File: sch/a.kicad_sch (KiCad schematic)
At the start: 1 part

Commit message: Update
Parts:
- added L? (x2): L, symbol Device:L
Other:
- moved on the sheet: L?
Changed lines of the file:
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@@
 (kicad_sch (version 20211123) (generator eeschema)
   (paper "A4")
-  (symbol (lib_id "Device:L") (at 132.08 100.33 0) (unit 1)
+  (symbol (lib_id "Device:L") (at 153.67 110.49 0) (unit 1)
     (in_bom yes) (on_board yes) (fields_autoplaced)
-    (property "Reference" "L?" (id 0) (at 133.35 99.0599 0)
+    (property "Reference" "L?" (id 0) (at 154.94 109.2199 0)
       (effects (font (size 1.27 1.27)) (justify left))
     )
-    (property "Value" "L" (id 1) (at 133.35 101.5999 0)
+    (property "Value" "L" (id 1) (at 154.94 111.7599 0)
       (effects (font (size 1.27 1.27)) (justify left))
     )
-    (property "Footprint" "" (id 2) (at 132.08 100.33 0)
+    (property "Footprint" "" (id 2) (at 153.67 110.49 0)
       (effects (font (size 1.27 1.27)) hide)
     )
-    (property "Datasheet" "~" (id 3) (at 132.08 100.33 0)
+    (property "Datasheet" "~" (id 3) (at 153.67 110.49 0)
       (effects (font (size 1.27 1.27)) hide)
     )
@@
     (pin "2")
   )
-  (sheet (at 142.24 93.98) (size 40.64 21.59) (fields_autoplaced)
+  (symbol (lib_id "Device:L") (at 158.75 110.49 0) (unit 1)
+    (in_bom yes) (on_board yes) (fields_autoplaced)
+    (property "Reference" "L?" (id 0) (at 160.02 109.2199 0)
+      (effects (font (size 1.27 1.27)) (justify left))
+    )
+    (property "Value" "L" (id 1) (at 160.02 111.7599 0)
+      (effects (font (size 1.27 1.27)) (justify left))
+    )
+    (property "Footprint" "" (id 2) (at 158.75 110.49 0)
+      (effects (font (size 1.27 1.27)) hide)
+    )
+    (property "Datasheet" "~" (id 3) (at 158.75 110.49 0)
+      (effects (font (size 1.27 1.27)) hide)
+    )
+    (pin "1")
+    (pin "2")
+  )
+  (symbol (lib_id "Device:L") (at 147.32 110.49 0) (unit 1)
+    (in_bom yes) (on_board yes) (fields_autoplaced)
+    (property "Reference" "L?" (id 0) (at 148.59 109.2199 0)
+      (effects (font (size 1.27 1.27)) (justify left))
+    )
+    (property "Value" "L" (id 1) (at 148.59 111.7599 0)
+      (effects (font (size 1.27 1.27)) (justify left))
+    )
+    (property "Footprint" "" (id 2) (at 147.32 110.49 0)
+      (effects (font (size 1.27 1.27)) hide)
+    )
+    (property "Datasheet" "~" (id 3) (at 147.32 110.49 0)
+      (effects (font (size 1.27 1.27)) hide)
+    )
+    (pin "1")
+    (pin "2")
+  )
+  (sheet (at 134.62 78.74) (size 40.64 21.59) (fields_autoplaced)
     (stroke (width 0.1524) (type solid) (color 0 0 0 0))
     (fill (color 0 0 0 0.0000))
-    (property "Sheet name" "B" (id 0) (at 142.24 93.2684 0)
+    (property "Sheet name" "B" (id 0) (at 134.62 78.0284 0)
       (effects (font (size 1.27 1.27)) (justify left bottom))
     )
-    (property "Sheet file" "b.kicad_sch" (id 1) (at 142.24 116.1546 0)
+    (property "Sheet file" "b.kicad_sch" (id 1) (at 134.62 100.9146 0)
       (effects (font (size 1.27 1.27)) (justify left top))
     )

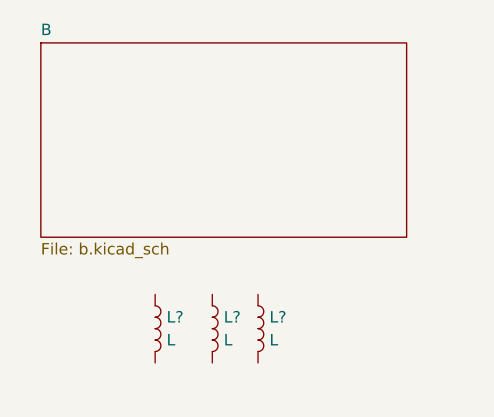
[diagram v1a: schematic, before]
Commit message: Add file and sheet instance with spaces. Anotate parts.
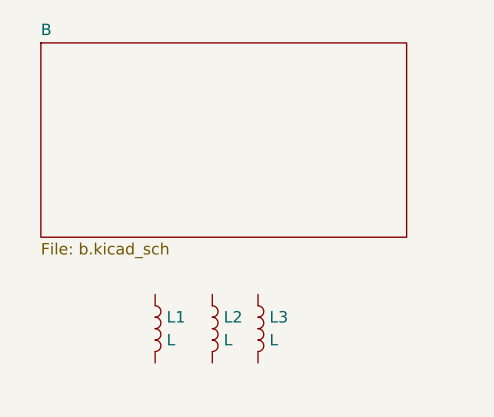
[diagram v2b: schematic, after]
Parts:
- gave numbers to parts that had none: 3
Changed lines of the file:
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@@
   (symbol (lib_id "Device:L") (at 153.67 110.49 0) (unit 1)
     (in_bom yes) (on_board yes) (fields_autoplaced)
-    (property "Reference" "L?" (id 0) (at 154.94 109.2199 0)
+    (property "Reference" "L2" (id 0) (at 154.94 109.2199 0)
       (effects (font (size 1.27 1.27)) (justify left))
     )
@@
   (symbol (lib_id "Device:L") (at 158.75 110.49 0) (unit 1)
     (in_bom yes) (on_board yes) (fields_autoplaced)
-    (property "Reference" "L?" (id 0) (at 160.02 109.2199 0)
+    (property "Reference" "L3" (id 0) (at 160.02 109.2199 0)
       (effects (font (size 1.27 1.27)) (justify left))
     )
@@
   (symbol (lib_id "Device:L") (at 147.32 110.49 0) (unit 1)
     (in_bom yes) (on_board yes) (fields_autoplaced)
-    (property "Reference" "L?" (id 0) (at 148.59 109.2199 0)
+    (property "Reference" "L1" (id 0) (at 148.59 109.2199 0)
       (effects (font (size 1.27 1.27)) (justify left))
     )
